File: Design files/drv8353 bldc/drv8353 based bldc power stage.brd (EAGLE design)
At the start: 127 x 127 mm, 110 parts, among them IC1 DRV8350RSRGZT, J3 2X6 FEMALE, J4 B06B-HCMKK

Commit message: started layout of power stage
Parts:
- removed BB2: (no value), busbar:TE3/2
- removed C1: 0.1uF, resistor:C0603K
- removed C10, C11, C12: 2200pF, rcl:C0603K
- removed C13: 1 uF, rcl:C1206K
- removed C14: .1 uF, resistor:C0805K
- removed C15, C16, C17: 1 uF, rcl:C0603K
- removed C18: .01uF, rcl:C0603K
- removed C19: 3600pF, rcl:C0603K
- removed C20: 2.2uF, rcl:C0805K
- removed C21: .047 uF, rcl:C0805K
- removed C22: 1 uF, resistor:C0603K
- removed C25: .1 uF, rcl:C0805K
- removed C26: 10 uF, rcl:C2220K
- removed C27: 1 uF, rcl:C0805K
- removed C28: .01 uF, rcl:C0603K
- removed C29: 4.7 uF, rcl:C1210K
- removed D4: DFLS1200, REV BLDC:DFLS1200
- removed IC1: DRV8350RSRGZT, REV BLDC:QFN50P700X700X100-49N
- removed J3: 2X6 FEMALE, pinhead:2X06
- removed J4: B06B-HCMKK, SamacSys_Parts:B06BHCMKK
- removed JP1: (no value), pinhead:1X02
- removed L3: 330 uH, REV BLDC:74404084331
- removed LDO: LP2992IM5-5.0_NOPB, SamacSys_Parts:SOT95P280X145-5N
- removed LED1: (no value), eagle-ltspice:LED_SML0603
- removed R1, R_FB1: 10k, rcl:R0603
- removed R10, R11, R12: 56, rcl:R0603
- removed R13: 107k, rcl:R0603
- removed R14: 274k, rcl:R0603
- removed R17: 2.61, rcl:R0603
- removed R2: 330, rcl:R0603
- removed R20: 1k, rcl:R0603
- removed R3: 5K, resistor:R0603
- removed R4, R5: 0, resistor:R0603
- removed R_FB2: 2.61k, rcl:R0603
- removed S1: RDT1034, switch:RDT1034
- removed SV1: (no value), pinhead:1X03
- removed TP10, TP11, TP12, TP15, TP19, TP32, TP33, TP34, TP36, TP40, TP5, TP6, TP7, TP8, TP9: TPB1,27, testpad:B1,27
- removed TVS_DIODE: TPD4S010DQAR, REV BLDC:TPD4S010DQAR
- removed U$1: ZENER, REV BLDC:SOD123
- removed U$2: BOOSTER_DOCK, REV BLDC:BOOSTER_DOCK
- added U$11, U$12, U$13, U$15, U$4, U$5: ZENER_PACK, REV BLDC:SOT23
- moved TP20 200.4 mm to (-97.8, 109.2)
- moved U$8 194.3 mm to (-85.1, 72.4)
- moved D3 184.9 mm to (-95.2, 101.6)
- moved U$19 180.1 mm to (-67.3, 47.0), turned to 0 degrees
- moved D1 179.6 mm to (-82.5, 101.6)
- moved D2 178.7 mm to (-88.9, 101.6)
- moved TP16 167.1 mm to (-85.1, 109.2)
- moved U$7 166.9 mm to (-58.4, 72.4)
- moved TP17 160.4 mm to (-91.4, 109.2)
- moved TP14 159.3 mm to (-78.7, 109.2)
- moved U$6 144.2 mm to (-31.8, 72.4)
- moved R28 142.9 mm to (-77.5, 102.9), turned to 0 degrees
- moved U$18 137.4 mm to (-44.5, 47.0), turned to 0 degrees
- moved R27 134.9 mm to (-71.1, 102.9), turned to 0 degrees
- moved R24 127.0 mm to (-64.8, 102.9), turned to 0 degrees
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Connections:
- removed net 3V3: J4.2, JP1.2, R1.2, R2.2, R20.2, U$2.1
- removed net AGND: IC1.27, R4.1, TP40.TP
- removed net BST: C18.2, IC1.45
- removed net CPH: C21.2, IC1.4
- removed net CPL: C21.1, IC1.3
- removed net CS: IC1.32, J3.10, U$2.19
- removed net DRV_VM: C25.1, C26.1, IC1.5, SV1.2, TP15.TP
- removed net ENABLE: IC1.33, R3.1, S1.B, U$2.11
- removed net FB: C19.2, IC1.48, R_FB1.1, R_FB2.2
- removed net HALL_A: J4.3, U$2.34
- removed net HALL_B: J4.4, U$2.33
- removed net HALL_C: J4.5, U$2.32
- removed net INHA: IC1.34, J3.11, U$2.40
- removed net INHB: IC1.36, J3.7, U$2.38
- removed net INHC: IC1.38, J3.6, U$2.36
- removed net INLA: IC1.35, J3.9, U$2.39
- removed net INLB: IC1.37, J3.8, U$2.37
- removed net INLC: IC1.39, J3.4, U$2.35
- removed net ISENA: C10.1, R10.1, U$2.27
- removed net ISENB: C11.1, R11.1, U$2.28
- removed net ISENC: C12.1, R12.1, U$2.29
- removed net MISO: IC1.29, J3.1, R20.1, U$2.14
- removed net MOSI: IC1.30, J3.3, U$2.15
- removed net N$1: C15.2, IC1.40
- removed net N$13: C28.2, LDO.4
- removed net N$14: C20.1, R17.1
- removed net N$16: LED1.A, R2.1
- removed net N$2: C29.2, JP1.1, LDO.5
- removed net N$20: C1.1, R3.2
- removed net NFAULT: IC1.28, LED1.C, R1.1, U$2.12
- removed net PGND: R5.1, TP19.TP, U$2.2
- removed net RCL: IC1.46, R13.2
- removed net RT/SD: IC1.47, R14.2
- removed net SCLK: IC1.31, J3.5, U$2.7
- removed net SW: C18.1, D4.LINE, IC1.42, L3.P$2
- removed net VBUCK: C19.1, C20.2, C27.2, L3.P$1, LDO.1, LDO.3, R_FB1.2, SV1.1, U$1.LINE
- removed net VCC: C17.2, IC1.44
- removed net VCP: C22.2, IC1.7
- removed net VGLS: C16.2, IC1.2
- net APHASE: now also U$5.2; no longer IC1.9, TP32.TP
- net BPHASE: now also U$11.2; no longer IC1.16, TP6.TP
- net CPHASE: now also U$13.2; no longer IC1.19, TP12.TP
- net GHA: now also U$5.1; no longer IC1.8, TP36.TP
- net GHB: now also U$11.1; no longer IC1.17, TP8.TP
- net GHC: now also U$13.1; no longer IC1.18, TP9.TP
- net GLA: now also U$4.1; no longer IC1.10, TP33.TP
- net GLB: now also U$12.1; no longer IC1.15, TP7.TP
- net GLC: now also U$15.1; no longer IC1.20, TP11.TP
- net GND: now also U$10.+, U$3.+, U$9.+; no longer BB2.1, BB2.2, C1.2, C10.2, C11.2, C12.2, C13.2, C14.1, C15.1, C16.1, C17.1, C25.2, C26.2, C27.1, C28.1, C29.1, D4.GND, IC1.1, IC1.41, IC1.49, J3.12, J3.2, J4.6, LDO.2, R13.1, R17.2, R4.2, R5.2, R_FB2.1, S1.A, S1.A1, TVS_DIODE.AGND, TVS_DIODE.GND, U$1.2, U$10.IP+1, U$10.IP+10, U$10.IP+11, U$10.IP+12, U$10.IP+13, U$10.IP+14, U$10.IP+15, U$10.IP+16, U$10.IP+17, U$10.IP+18, U$10.IP+2, U$10.IP+3, U$10.IP+4, U$10.IP+5, U$10.IP+6, U$10.IP+7, U$10.IP+8, U$10.IP+9, U$2.20, U$2.22, U$3.IP+1, U$3.IP+10, U$3.IP+11, U$3.IP+12, U$3.IP+13, U$3.IP+14, U$3.IP+15, U$3.IP+16, U$3.IP+17, U$3.IP+18, U$3.IP+2, U$3.IP+3, U$3.IP+4, U$3.IP+5, U$3.IP+6, U$3.IP+7, U$3.IP+8, U$3.IP+9, U$9.IP+1, U$9.IP+10, U$9.IP+11, U$9.IP+12, U$9.IP+13, U$9.IP+14, U$9.IP+15, U$9.IP+16, U$9.IP+17, U$9.IP+18, U$9.IP+2, U$9.IP+3, U$9.IP+4, U$9.IP+5, U$9.IP+6, U$9.IP+7, U$9.IP+8, U$9.IP+9
- net SLA: now also U$3.-, U$4.2; no longer IC1.11, TP34.TP, U$3.IP-1, U$3.IP-10, U$3.IP-11, U$3.IP-12, U$3.IP-13, U$3.IP-14, U$3.IP-15, U$3.IP-16, U$3.IP-17, U$3.IP-18, U$3.IP-2, U$3.IP-3, U$3.IP-4, U$3.IP-5, U$3.IP-6, U$3.IP-7, U$3.IP-8, U$3.IP-9
- net SLB: now also U$12.2, U$9.-; no longer IC1.14, TP5.TP, U$9.IP-1, U$9.IP-10, U$9.IP-11, U$9.IP-12, U$9.IP-13, U$9.IP-14, U$9.IP-15, U$9.IP-16, U$9.IP-17, U$9.IP-18, U$9.IP-2, U$9.IP-3, U$9.IP-4, U$9.IP-5, U$9.IP-6, U$9.IP-7, U$9.IP-8, U$9.IP-9
- net SLC: now also U$10.-, U$15.2; no longer IC1.21, TP10.TP, U$10.IP-1, U$10.IP-10, U$10.IP-11, U$10.IP-12, U$10.IP-13, U$10.IP-14, U$10.IP-15, U$10.IP-16, U$10.IP-17, U$10.IP-18, U$10.IP-2, U$10.IP-3, U$10.IP-4, U$10.IP-5, U$10.IP-6, U$10.IP-7, U$10.IP-8, U$10.IP-9
- net SOA: no longer R10.2
- net SOB: no longer R11.2
- net SOC: no longer R12.2
- net VDRAIN: no longer C13.1, C14.2, C22.1, IC1.43, IC1.6, R14.1, SV1.3
- net VSENA: no longer TVS_DIODE.D1+, TVS_DIODE.P$6, U$2.30
- net VSENB: no longer TVS_DIODE.D0-, TVS_DIODE.P$7, U$2.25
- net VSENC: no longer TVS_DIODE.D0+, TVS_DIODE.P$8, U$2.26
- net VSENVM: no longer TVS_DIODE.D1-, TVS_DIODE.P$5, U$2.23
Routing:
- net APHASE: track 177.7 -> 0.00 mm, vias 115 -> 0
- net BPHASE: track 132.5 -> 0.00 mm, vias 114 -> 0
- net 3V3: track 103.0 -> 0.00 mm, vias 2 -> 0
- net SCLK: track 79.1 -> 0.00 mm, vias 2 -> 0
- net VDRAIN: track 78.3 -> 0.00 mm, vias 100 -> 0
- net CPHASE: track 73.7 -> 0.00 mm, vias 110 -> 0
- net GHA: track 63.4 -> 0.00 mm
- net CS: track 58.9 -> 0.00 mm, vias 1 -> 0
- net GLC: track 56.6 -> 0.00 mm
- net INHA: track 53.5 -> 0.00 mm, vias 1 -> 0
- net INHB: track 53.3 -> 0.00 mm, vias 1 -> 0
- net ENABLE: track 52.3 -> 0.00 mm
- net INLB: track 51.3 -> 0.00 mm, vias 1 -> 0
- net INLA: track 51.3 -> 0.00 mm, vias 1 -> 0
- net INHC: track 49.9 -> 0.00 mm, vias 1 -> 0
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- removed copper zone on layer 1, net 3V3
- removed copper zone on layer 1, net APHASE
- removed copper zone on layer 15, net APHASE
- removed copper zone on layer 16, net APHASE
- removed copper zone on layer 2, net APHASE
- removed copper zone on layer 1, net BPHASE
- removed copper zone on layer 15, net BPHASE
- removed copper zone on layer 16, net BPHASE
- removed copper zone on layer 2, net BPHASE
- removed copper zone on layer 1, net CPHASE
- removed copper zone on layer 15, net CPHASE
- removed copper zone on layer 16, net CPHASE
- removed copper zone on layer 2, net CPHASE
- removed copper zone on layer 1, net GND
- removed copper zone on layer 15, net GND
- removed copper zone on layer 16, net GND
- removed copper zone on layer 2, net GND
- removed copper zone on layer 1, net N$15
- removed copper zone on layer 15, net N$15
- removed copper zone on layer 16, net N$15
- removed copper zone on layer 2, net N$15
- removed copper zone on layer 1, net SLA
- removed copper zone on layer 1, net SLB
- removed copper zone on layer 1, net SLC
- removed copper zone on layer 1, net SW
- removed copper zone on layer 1, net VBUCK
- removed copper zone on layer 1, net VDRAIN
- removed copper zone on layer 15, net VDRAIN
- removed copper zone on layer 16, net VDRAIN
- removed copper zone on layer 2, net VDRAIN
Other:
- board size 127 x 127 mm -> 63.5 x 127 mm
- board text removed: "AGND"
- board text removed: "APHASE"
- board text removed: "BPHASE"
- board text removed: "CPHASE"
- board text removed: "DRVM"
- board text removed: "GHA"
- board text removed: "GHB"
- board text removed: "GHC"
- board text removed: "GLA"
- board text removed: "GLB"
- board text removed: "GLC"
- board text removed: "GND"
- board text removed: "MADE FOR SEM BY RICE ELECTRIC VEHICLE 2019-2020"
- board text removed: "PGND"
- board text removed: "SNA"
- board text removed: "SNB"
- board text removed: "SNC"
- board text removed: "SOA"
- board text removed: "SOB"
- board text removed: "SOC"
- board text removed: "SPA"
- board text removed: "SPB"
- board text removed: "SPC"
- board text removed: "VBATT"

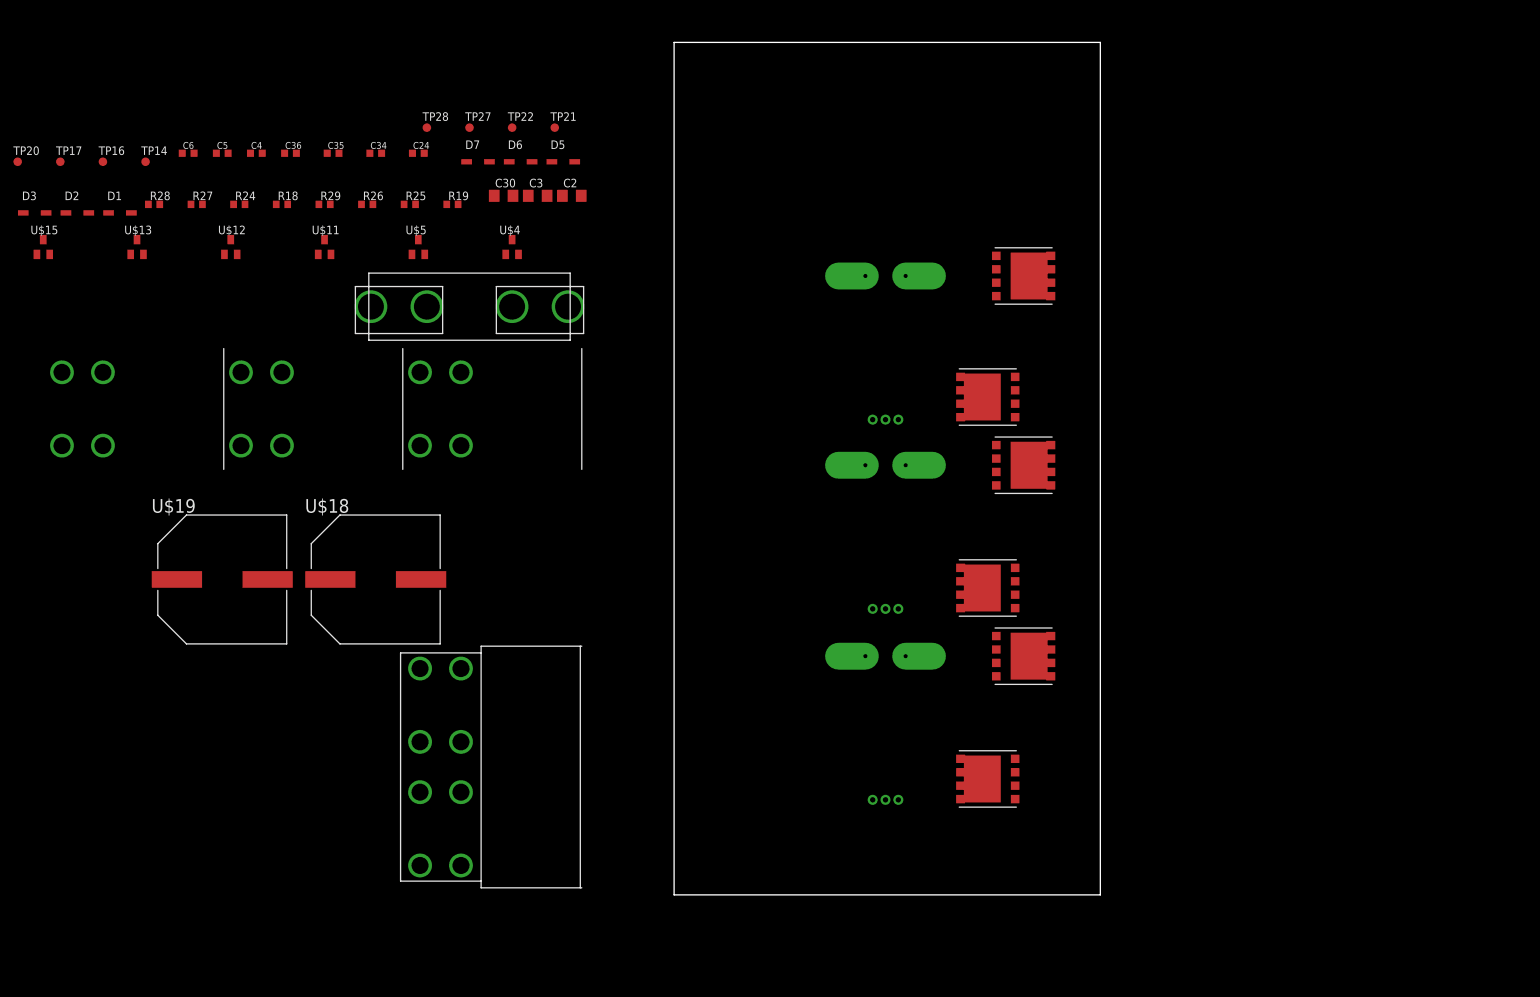
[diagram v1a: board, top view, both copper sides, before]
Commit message: large components tenetively placed
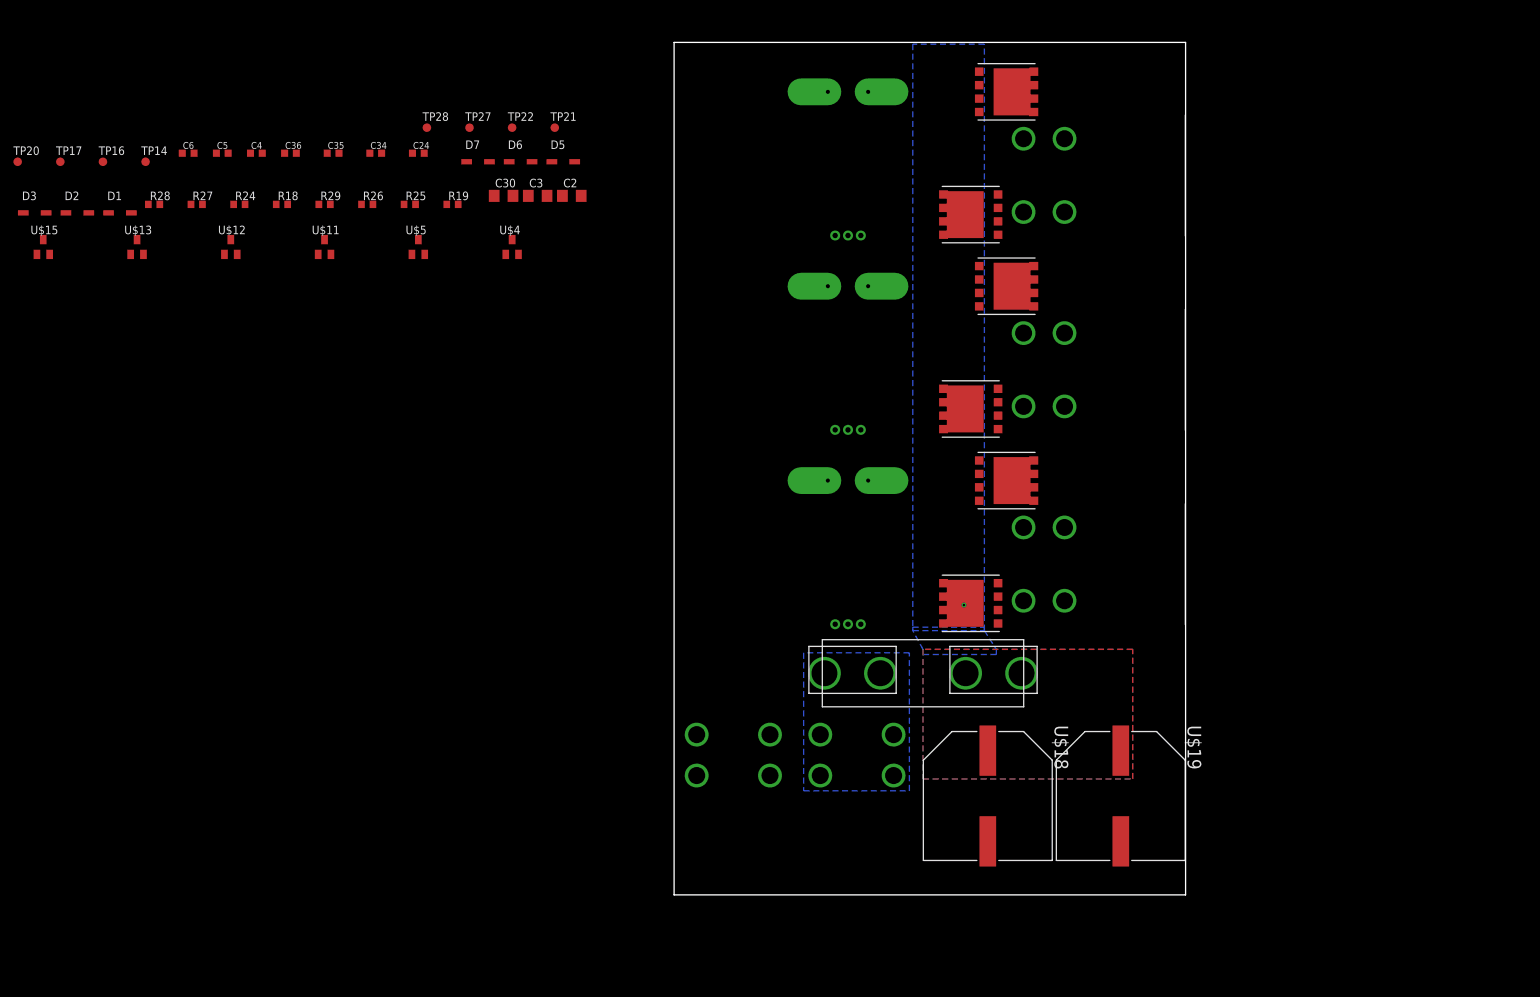
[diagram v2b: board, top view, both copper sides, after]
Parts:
- moved U$8 145.1 mm to (58.2, 49.3)
- moved U$19 137.7 mm to (66.5, 14.7), turned to 270 degrees
- moved U$7 116.7 mm to (58.2, 78.2)
- moved U$18 96.7 mm to (46.7, 14.7), turned to 270 degrees
- moved U$6 96.4 mm to (58.2, 107.2)
- moved F1 86.9 mm to (37.1, 33.0), turned to 180 degrees
- moved U$16 49.8 mm to (18.0, 17.8), flipped to the bottom, turned to 270 degrees
- moved U$10 28.0 mm to (25.9, 119.6)
- moved U$24 27.5 mm to (49.5, 119.6)
- moved U$23 27.3 mm to (44.2, 101.3)
- moved U$9 27.2 mm to (25.9, 90.7)
- moved U$21 26.8 mm to (49.5, 90.7)
- moved U$22 26.8 mm to (44.2, 72.4)
- moved U$3 26.8 mm to (25.9, 61.7)
- moved U$14 26.3 mm to (44.2, 43.4)
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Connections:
- net GND: now also U$16.+1, U$16.+2, U$16.+3, U$16.+4; no longer U$16.-1, U$16.-2, U$16.-3, U$16.-4
- net N$15: now also U$16.-1, U$16.-2, U$16.-3, U$16.-4; no longer U$16.+1, U$16.+2, U$16.+3, U$16.+4
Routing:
- added copper zone on layer 16, net N$15
- added copper zone on layer 1, net VDRAIN
- added copper zone on layer 15, net VDRAIN
- added copper zone on layer 16, net VDRAIN
- added copper zone on layer 2, net VDRAIN
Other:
- board size 63.5 x 127 mm -> 76.2 x 127 mm

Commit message: created tenetive board connection part, did some initial routing
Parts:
- removed C24: 0.047 uF, rcl:C0603K
- removed C34, C35, C36: .047uF, rcl:C0603K
- removed R18, R24, R27, R28: 383k, rcl:R0603
- removed R19, R25, R26, R29: 9.76k, rcl:R0603
- removed U$20, U$21, U$22, U$23, U$24: NVMTS1D2N08H, REV BLDC:PQFN88
- added U$1, U$17, U$2, U$25, U$26, U$27: IAUT300N08S5N014, SamacSys_Parts:PG-HSOF-8-1_MODIFIED
- U$14: value NVMTS1D2N08H -> POWER_STAGE_CONNECTOR; device REV BLDC:PQFN88 -> REV BLDC:POWER_STAGE_CONNECTION
- moved TP17 160.8 mm to (57.9, 49.5)
- moved D3 146.9 mm to (51.3, 111.0)
- moved U$15 145.3 mm to (48.8, 123.7), turned to 90 degrees
- moved D1 142.4 mm to (51.3, 53.1)
- moved D2 141.6 mm to (51.3, 82.0)
- moved TP16 138.3 mm to (27.2, 28.4)
- moved U$13 136.9 mm to (56.9, 98.8), turned to 180 degrees
- moved TP20 115.6 mm to (17.3, 120.1)
- moved U$12 114.8 mm to (48.8, 94.7), turned to 90 degrees
- moved C4 113.3 mm to (28.2, 42.2)
- moved U$11 112.2 mm to (56.9, 69.8), turned to 180 degrees
- moved U$5 110.1 mm to (56.9, 40.9), turned to 180 degrees
- moved C5 103.3 mm to (28.2, 71.1)
- moved C6 101.1 mm to (28.2, 100.1)
- moved TP14 97.4 mm to (17.0, 91.2)
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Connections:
- removed net VSENA: C34.1, R24.1, R25.2
- removed net VSENB: C35.1, R26.2, R27.1
- removed net VSENC: C36.1, R28.1, R29.2
- removed net VSENVM: C24.1, R18.1, R19.2
- new net N$1: U$14.VDRAIN
- new net N$10: U$14.GHB
- new net N$11: U$14.GHC
- new net N$12: U$14.CPHASE
- new net N$13: U$14.GLC
- new net N$14: U$14.SLC
- new net N$16: U$14.SOC
- new net N$17: U$14.SOB
- new net N$18: U$14.SOA
- new net N$19: U$14.CPHASE2
- new net N$2: U$14.GND, U$14.GND2
- new net N$20: U$14.BPHASE2
- new net N$21: U$14.APHASE2
- new net N$22: U$14.VDRAIN2
- new net N$23: U$14.5V
- new net N$3: U$14.GHA
- new net N$4: U$14.APHASE
- new net N$5: U$14.GLA
- new net N$6: U$14.SLA
- new net N$7: U$14.SLB
- new net N$8: U$14.GLB
- new net N$9: U$14.BPHASE
- net APHASE: now also U$1.11, U$1.12, U$1.13, U$1.14, U$1.15, U$1.3, U$1.4, U$1.5, U$1.6, U$1.7, U$1.8, U$2.16, U$2.17, U$2.18, U$2.19, U$2.9, U$5.1; no longer R24.2, U$14.S1, U$14.S2, U$14.S3, U$20.D1, U$20.D2, U$20.D3, U$20.D4, U$20.DT, U$5.2
- net BPHASE: now also U$11.1, U$17.16, U$17.17, U$17.18, U$17.19, U$17.9, U$25.11, U$25.12, U$25.13, U$25.14, U$25.15, U$25.3, U$25.4, U$25.5, U$25.6, U$25.7, U$25.8; no longer R27.2, U$11.2, U$21.D1, U$21.D2, U$21.D3, U$21.D4, U$21.DT, U$22.S1, U$22.S2, U$22.S3
- net CPHASE: now also U$13.1, U$26.11, U$26.12, U$26.13, U$26.14, U$26.15, U$26.3, U$26.4, U$26.5, U$26.6, U$26.7, U$26.8, U$27.16, U$27.17, U$27.18, U$27.19, U$27.9; no longer R28.2, U$13.2, U$23.S1, U$23.S2, U$23.S3, U$24.D1, U$24.D2, U$24.D3, U$24.D4, U$24.DT
- net GHA: now also U$1.1, U$5.2; no longer U$14.G, U$5.1
- net GHB: now also U$11.2, U$25.1; no longer U$11.1, U$22.G
- net GHC: now also U$13.2, U$26.1; no longer U$13.1, U$23.G
- net GLA: now also U$2.1, U$4.2; no longer U$20.G, U$4.1
- net GLB: now also U$12.2, U$17.1; no longer U$12.1, U$21.G
- net GLC: now also U$15.2, U$27.1; no longer U$15.1, U$24.G
- net GND: no longer C24.2, C34.2, C35.2, C36.2, R19.1, R25.1, R26.1, R29.1
- net SLA: now also U$2.11, U$2.12, U$2.13, U$2.14, U$2.15, U$2.3, U$2.4, U$2.5, U$2.6, U$2.7, U$2.8, U$4.1; no longer U$20.S1, U$20.S2, U$20.S3, U$4.2
- net SLB: now also U$12.1, U$17.11, U$17.12, U$17.13, U$17.14, U$17.15, U$17.3, U$17.4, U$17.5, U$17.6, U$17.7, U$17.8; no longer U$12.2, U$21.S1, U$21.S2, U$21.S3
- net SLC: now also U$15.1, U$27.11, U$27.12, U$27.13, U$27.14, U$27.15, U$27.3, U$27.4, U$27.5, U$27.6, U$27.7, U$27.8; no longer U$15.2, U$24.S1, U$24.S2, U$24.S3
- net VDRAIN: now also U$1.16, U$1.17, U$1.18, U$1.19, U$1.9, U$25.16, U$25.17, U$25.18, U$25.19, U$25.9, U$26.16, U$26.17, U$26.18, U$26.19, U$26.9; no longer R18.2, U$14.D1, U$14.D2, U$14.D3, U$14.D4, U$14.DT, U$22.D1, U$22.D2, U$22.D3, U$22.D4, U$22.DT, U$23.D1, U$23.D2, U$23.D3, U$23.D4, U$23.DT
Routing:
- added copper zone on layer 1, net APHASE
- added copper zone on layer 1, net BPHASE
- added copper zone on layer 1, net CPHASE
- added copper zone on layer 1, net GHA
- added copper zone on layer 1, net GHB
- added copper zone on layer 1, net GHC
- added copper zone on layer 1, net GLA
- added copper zone on layer 1, net GLB
- added copper zone on layer 1, net GLC
- added copper zone on layer 16, net GND
- added copper zone on layer 1, net SLA
- added copper zone on layer 1, net SLB
- added copper zone on layer 1, net SLC
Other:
- board size 76.2 x 127 mm -> 85.1 x 127 mm

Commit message: finished most of power stage routing
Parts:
- moved TP14 5.04 mm to (20.8, 87.9)
- moved TP27 0.25 mm to (17.0, 62.2)
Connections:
- removed net N$1: U$14.VDRAIN
- removed net N$10: U$14.GHB
- removed net N$11: U$14.GHC
- removed net N$12: U$14.CPHASE
- removed net N$13: U$14.GLC
- removed net N$14: U$14.SLC
- removed net N$16: U$14.SOC
- removed net N$17: U$14.SOB
- removed net N$18: U$14.SOA
- removed net N$19: U$14.CPHASE2
- removed net N$2: U$14.GND, U$14.GND2
- removed net N$20: U$14.BPHASE2
- removed net N$21: U$14.APHASE2
- removed net N$22: U$14.VDRAIN2
- removed net N$23: U$14.5V
- removed net N$3: U$14.GHA
- removed net N$4: U$14.APHASE
- removed net N$5: U$14.GLA
- removed net N$6: U$14.SLA
- removed net N$7: U$14.SLB
- removed net N$8: U$14.GLB
- removed net N$9: U$14.BPHASE
- net 5V: now also U$14.5V
- net APHASE: now also U$14.APHASE, U$14.APHASE2
- net BPHASE: now also U$14.BPHASE, U$14.BPHASE2
- net CPHASE: now also U$14.CPHASE, U$14.CPHASE2
- net GHA: now also U$14.GHA
- net GHB: now also U$14.GHB
- net GHC: now also U$14.GHC
- net GLA: now also U$14.GLA
- net GLB: now also U$14.GLB
- net GLC: now also U$14.GLC
- net GND: now also U$14.GND, U$14.GND2
- net SLA: now also U$14.SLA
- net SLB: now also U$14.SLB
- net SLC: now also U$14.SLC
- net SOA: now also U$14.SOA
- net SOB: now also U$14.SOB
- net SOC: now also U$14.SOC
- net VDRAIN: now also U$14.VDRAIN, U$14.VDRAIN2
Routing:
- net APHASE: track 0.00 -> 233.2 mm
- net BPHASE: track 0.00 -> 204.2 mm, vias 0 -> 4
- net CPHASE: track 0.00 -> 143.9 mm
- net 5V: track 0.00 -> 120.8 mm, vias 0 -> 1
- net VDRAIN: track 0.00 -> 106.1 mm, vias 0 -> 1
- net GLB: track 0.00 -> 103.9 mm, vias 0 -> 2
- net GND: track 0.00 -> 100.6 mm
- net GLC: track 0.00 -> 99.8 mm
- net SLC: track 0.00 -> 71.1 mm, vias 0 -> 4
- net GHC: track 0.00 -> 68.8 mm
- net GHA: track 0.00 -> 67.3 mm
- net SLB: track 0.00 -> 56.6 mm
- net GHB: track 0.00 -> 55.8 mm, vias 0 -> 4
- net SOA: track 0.00 -> 55.7 mm, vias 0 -> 1
- net GLA: track 0.00 -> 47.4 mm
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- added copper zone on layer 1, net N$15
- added copper zone on layer 15, net N$15
- added copper zone on layer 2, net N$15
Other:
- board size 85.1 x 127 mm -> 85.1 x 131.3 mm

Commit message: more routing
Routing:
- net GND: track 100.6 -> 122.9 mm, vias 0 -> 8
- net 5V: track 120.8 -> 128.0 mm, vias 1 -> 4
- net VDRAIN: vias 1 -> 4
- added copper zone on layer 1, net GND
- added copper zone on layer 15, net GND
- added copper zone on layer 2, net GND

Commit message: beefed up some planes
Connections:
- net APHASE: now also U$1.10, U$1.2
- net BPHASE: now also U$25.10, U$25.2
- net CPHASE: now also U$26.10, U$26.2
- net SLA: now also U$2.10, U$2.2
- net SLB: now also U$17.10, U$17.2
- net SLC: now also U$27.10, U$27.2
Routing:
- net GND: track 122.9 -> 135.2 mm
- net SLB: track 56.6 -> 64.9 mm
- net SLA: track 46.9 -> 55.1 mm
- net SLC: track 71.1 -> 79.3 mm
- net GLC: track 99.8 -> 96.8 mm
- net 5V: vias 4 -> 5
- added copper zone on layer 15, net APHASE
- added copper zone on layer 16, net APHASE
- added copper zone on layer 2, net APHASE
- added copper zone on layer 15, net BPHASE
- added copper zone on layer 16, net BPHASE
- added copper zone on layer 2, net BPHASE
- added copper zone on layer 15, net CPHASE
- added copper zone on layer 16, net CPHASE
- added copper zone on layer 2, net CPHASE
